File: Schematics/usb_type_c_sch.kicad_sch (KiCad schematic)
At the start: 4 parts, among them J2 USB_C_Receptacle

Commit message: began routing
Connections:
- net D+: now also D1.4; no longer D1.1
- net D-: now also D1.6; no longer D1.3
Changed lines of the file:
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@@
+	)
+	(junction
+		(at 151.13 81.28)
+		(diameter 0)
+		(color 0 0 0 0)
+	)
+	(junction
+		(at 121.92 134.62)
+		(diameter 0)
+		(color 0 0 0 0)
 	)
 	(junction
@@
 	)
 	(junction
-		(at 121.92 134.62)
-		(diameter 0)
-		(color 0 0 0 0)
-	)
-	(junction
-		(at 149.86 81.28)
-		(diameter 0)
-		(color 0 0 0 0)
-	)
-	(junction
 		(at 147.32 81.28)
 		(diameter 0)
@@
 	(wire
 		(pts
-			(xy 147.32 81.28) (xy 149.86 81.28)
+			(xy 147.32 81.28) (xy 151.13 81.28)
 		)
 		(stroke
@@
 	(wire
 		(pts
-			(xy 153.67 86.36) (xy 160.02 86.36)
-		)
-		(stroke
-			(width 0)
-			(type default)
-		)
-	)
-	(wire
-		(pts
 			(xy 193.04 82.55) (xy 193.04 83.82)
 		)
@@
 	(wire
 		(pts
+			(xy 158.75 81.28) (xy 160.02 81.28)
+		)
+		(stroke
+			(width 0)
+			(type default)
+		)
+	)
+	(wire
+		(pts
 			(xy 147.32 80.01) (xy 147.32 81.28)
 		)
@@
 	(wire
 		(pts
-			(xy 149.86 81.28) (xy 153.67 81.28)
-		)
-		(stroke
-			(width 0)
-			(type default)
-		)
-	)
-	(wire
-		(pts
 			(xy 140.97 80.01) (xy 147.32 80.01)
 		)
@@
 	(wire
 		(pts
-			(xy 149.86 83.82) (xy 160.02 83.82)
+			(xy 151.13 81.28) (xy 151.13 78.74)
+		)
+		(stroke
+			(width 0)
+			(type default)
+		)
+	)
+	(wire
+		(pts
+			(xy 158.75 86.36) (xy 158.75 81.28)
 		)
 		(stroke
@@
 	(wire
 		(pts
+			(xy 151.13 78.74) (xy 160.02 78.74)
+		)
+		(stroke
+			(width 0)
+			(type default)
+		)
+	)
+	(wire
+		(pts
 			(xy 147.32 82.55) (xy 140.97 82.55)
 		)
@@
 	(wire
 		(pts
-			(xy 149.86 81.28) (xy 149.86 83.82)
-		)
-		(stroke
-			(width 0)
-			(type default)
-		)
-	)
-	(wire
-		(pts
 			(xy 144.78 63.5) (xy 144.78 67.31)
 		)
@@
 	(wire
 		(pts
+			(xy 151.13 81.28) (xy 153.67 81.28)
+		)
+		(stroke
+			(width 0)
+			(type default)
+		)
+	)
+	(wire
+		(pts
 			(xy 147.32 81.28) (xy 147.32 82.55)
 		)
 		(stroke
+			(width 0)
+			(type default)
+		)
+	)
+	(wire
+		(pts
+			(xy 153.67 86.36) (xy 158.75 86.36)
+		)
+		(stroke

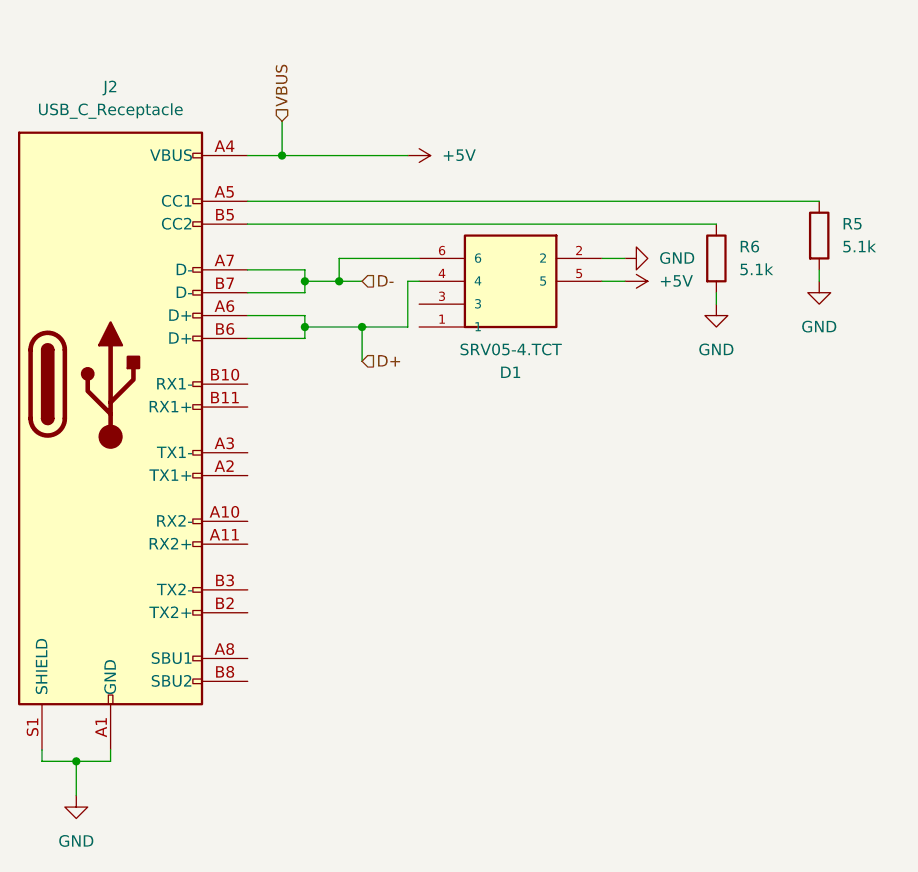
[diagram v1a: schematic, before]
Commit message: fixing routing redefining layout
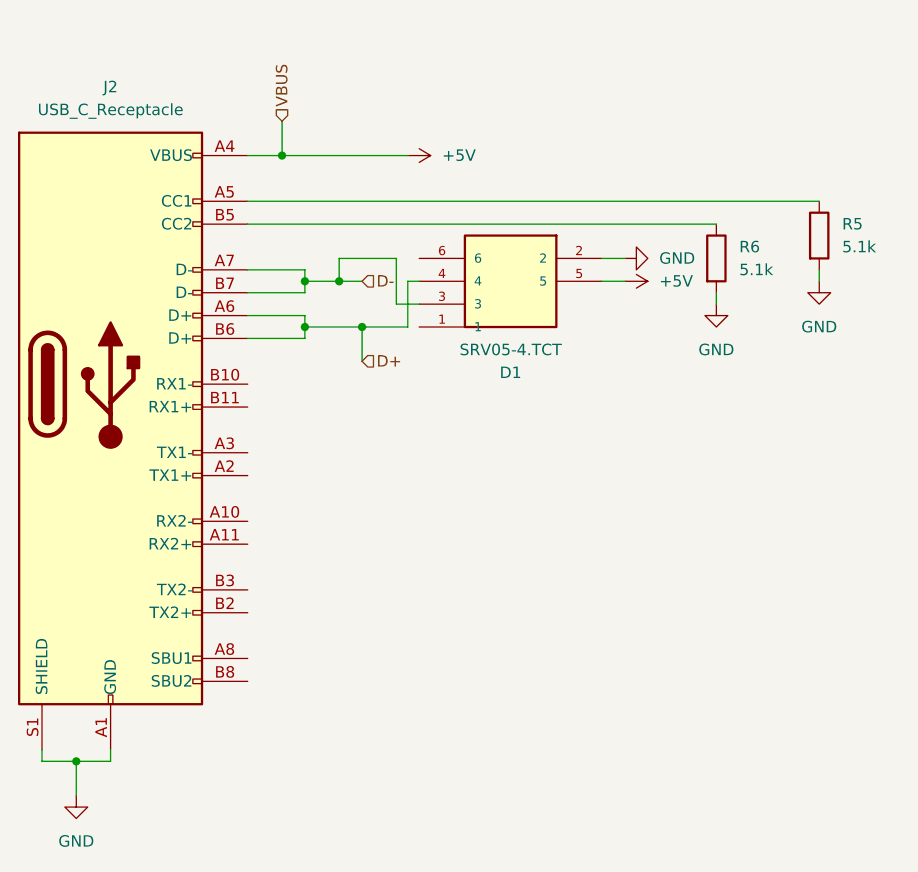
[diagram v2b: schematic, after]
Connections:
- net D-: now also D1.3; no longer D1.6
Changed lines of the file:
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@@
+	(wire
+		(pts
+			(xy 157.48 78.74) (xy 157.48 83.82)
+		)
+		(stroke
+			(width 0)
+			(type default)
+		)
+	)
 	(wire
 		(pts
@@
 	(wire
 		(pts
+			(xy 147.32 80.01) (xy 147.32 81.28)
+		)
+		(stroke
+			(width 0)
+			(type default)
+		)
+	)
+	(wire
+		(pts
+			(xy 140.97 67.31) (xy 144.78 67.31)
+		)
+		(stroke
+			(width 0)
+			(type default)
+		)
+	)
+	(wire
+		(pts
+			(xy 151.13 78.74) (xy 157.48 78.74)
+		)
+		(stroke
+			(width 0)
+			(type default)
+		)
+	)
+	(wire
+		(pts
+			(xy 140.97 85.09) (xy 147.32 85.09)
+		)
+		(stroke
+			(width 0)
+			(type default)
+		)
+	)
+	(wire
+		(pts
+			(xy 147.32 86.36) (xy 147.32 87.63)
+		)
+		(stroke
+			(width 0)
+			(type default)
+		)
+	)
+	(wire
+		(pts
+			(xy 140.97 74.93) (xy 193.04 74.93)
+		)
+		(stroke
+			(width 0)
+			(type default)
+		)
+	)
+	(wire
+		(pts
+			(xy 121.92 134.62) (xy 121.92 138.43)
+		)
+		(stroke
+			(width 0)
+			(type default)
+		)
+	)
+	(wire
+		(pts
 			(xy 158.75 81.28) (xy 160.02 81.28)
 		)
@@
 	(wire
 		(pts
-			(xy 147.32 80.01) (xy 147.32 81.28)
-		)
-		(stroke
-			(width 0)
-			(type default)
-		)
-	)
-	(wire
-		(pts
-			(xy 140.97 67.31) (xy 144.78 67.31)
-		)
-		(stroke
-			(width 0)
-			(type default)
-		)
-	)
-	(wire
-		(pts
-			(xy 140.97 85.09) (xy 147.32 85.09)
-		)
-		(stroke
-			(width 0)
-			(type default)
-		)
-	)
-	(wire
-		(pts
-			(xy 147.32 86.36) (xy 147.32 87.63)
-		)
-		(stroke
-			(width 0)
-			(type default)
-		)
-	)
-	(wire
-		(pts
-			(xy 140.97 74.93) (xy 193.04 74.93)
-		)
-		(stroke
-			(width 0)
-			(type default)
-		)
-	)
-	(wire
-		(pts
-			(xy 121.92 134.62) (xy 121.92 138.43)
-		)
-		(stroke
-			(width 0)
-			(type default)
-		)
-	)
-	(wire
-		(pts
 			(xy 140.97 80.01) (xy 147.32 80.01)
 		)
@@
 	(wire
 		(pts
+			(xy 153.67 90.17) (xy 153.67 86.36)
+		)
+		(stroke
+			(width 0)
+			(type default)
+		)
+	)
+	(wire
+		(pts
+			(xy 118.11 134.62) (xy 121.92 134.62)
+		)
+		(stroke
+			(width 0)
+			(type default)
+		)
+	)
+	(wire
+		(pts
+			(xy 147.32 85.09) (xy 147.32 86.36)
+		)
+		(stroke
+			(width 0)
+			(type default)
+		)
+	)
+	(wire
+		(pts
+			(xy 182.88 78.74) (xy 180.34 78.74)
+		)
+		(stroke
+			(width 0)
+			(type default)
+		)
+	)
+	(wire
+		(pts
+			(xy 204.47 80.01) (xy 204.47 81.28)
+		)
+		(stroke
+			(width 0)
+			(type default)
+		)
+	)
+	(wire
+		(pts
+			(xy 118.11 134.62) (xy 118.11 133.35)
+		)
+		(stroke
+			(width 0)
+			(type default)
+		)
+	)
+	(wire
+		(pts
+			(xy 147.32 82.55) (xy 140.97 82.55)
+		)
+		(stroke
+			(width 0)
+			(type default)
+		)
+	)
+	(wire
+		(pts
+			(xy 144.78 63.5) (xy 144.78 67.31)
+		)
+		(stroke
+			(width 0)
+			(type default)
+		)
+	)
+	(wire
+		(pts
+			(xy 125.73 134.62) (xy 125.73 133.35)
+		)
+		(stroke
+			(width 0)
+			(type default)
+		)
+	)
+	(wire
+		(pts
+			(xy 151.13 81.28) (xy 153.67 81.28)
+		)
+		(stroke
+			(width 0)
+			(type default)
+		)
+	)
+	(wire
+		(pts
+			(xy 157.48 83.82) (xy 160.02 83.82)
+		)
+		(stroke
+			(width 0)
+			(type default)
+		)
+	)
+	(wire
+		(pts
 			(xy 158.75 86.36) (xy 158.75 81.28)
 		)
 		(stroke
-			(width 0)
-			(type default)
-		)
-	)
-	(wire
-		(pts
-			(xy 153.67 90.17) (xy 153.67 86.36)
-		)
-		(stroke
-			(width 0)
-			(type default)
-		)
-	)
-	(wire
-		(pts
-			(xy 118.11 134.62) (xy 121.92 134.62)
-		)
-		(stroke
-			(width 0)
-			(type default)
-		)
-	)
-	(wire
-		(pts
-			(xy 147.32 85.09) (xy 147.32 86.36)
-		)
-		(stroke
-			(width 0)
-			(type default)
-		)
-	)
-	(wire
-		(pts
-			(xy 182.88 78.74) (xy 180.34 78.74)
-		)
-		(stroke
-			(width 0)
-			(type default)
-		)
-	)
-	(wire
-		(pts
-			(xy 204.47 80.01) (xy 204.47 81.28)
-		)
-		(stroke
-			(width 0)
-			(type default)
-		)
-	)
-	(wire
-		(pts
-			(xy 118.11 134.62) (xy 118.11 133.35)
-		)
-		(stroke
-			(width 0)
-			(type default)
-		)
-	)
-	(wire
-		(pts
-			(xy 151.13 78.74) (xy 160.02 78.74)
-		)
-		(stroke
-			(width 0)
-			(type default)
-		)
-	)
-	(wire
-		(pts
-			(xy 147.32 82.55) (xy 140.97 82.55)
-		)
-		(stroke
-			(width 0)
-			(type default)
-		)
-	)
-	(wire
-		(pts
-			(xy 144.78 63.5) (xy 144.78 67.31)
-		)
-		(stroke
-			(width 0)
-			(type default)
-		)
-	)
-	(wire
-		(pts
-			(xy 125.73 134.62) (xy 125.73 133.35)
-		)
-		(stroke
-			(width 0)
-			(type default)
-		)
-	)
-	(wire
-		(pts
-			(xy 151.13 81.28) (xy 153.67 81.28)
-		)
-		(stroke

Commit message: routing taking place only USB to do
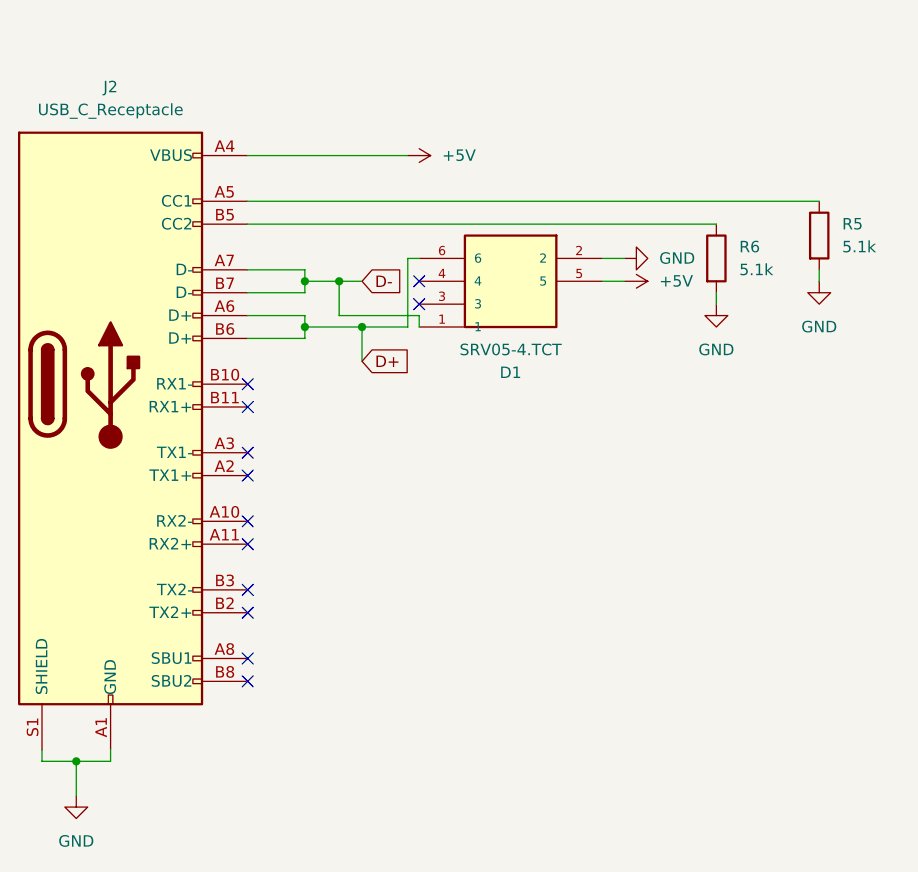
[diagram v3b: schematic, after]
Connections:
- net D+: now also D1.6; no longer D1.4
- net D-: now also D1.1; no longer D1.3
- no-connect marks 0 -> 12

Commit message: Cleaned up schematic added ocilator added jtag 10 pin begining routing again
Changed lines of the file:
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@@
 		)
 	)
-	(global_label "D-"
+	(hierarchical_label "D-"
 		(shape input)
 		(at 153.67 81.28 0)
-		(fields_autoplaced yes)
 		(effects
 			(font
@@
 			(justify left)
 		)
-		(property "Intersheetrefs" "${INTERSHEET_REFS}"
-			(at 159.4976 81.28 0)
-			(effects
-				(font
-					(size 1.27 1.27)
-				)
-				(justify left)
-				(hide yes)
-			)
-		)
 	)
-	(global_label "D+"
+	(hierarchical_label "D+"
 		(shape input)
 		(at 153.67 90.17 0)
-		(fields_autoplaced yes)
 		(effects
 			(font
@@
 			(justify left)
 		)
-		(property "Intersheetrefs" "${INTERSHEET_REFS}"
-			(at 159.4976 90.17 0)
-			(effects
-				(font
-					(size 1.27 1.27)
-				)
-				(justify left)
-				(hide yes)
-			)
-		)
 	)

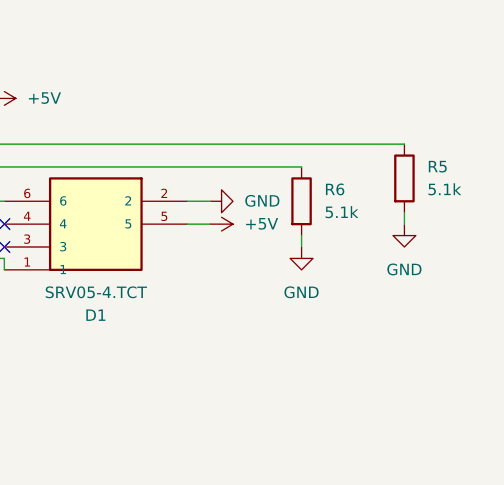
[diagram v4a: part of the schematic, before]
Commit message: added LCSC numbers and generated BOM, fixed schematic
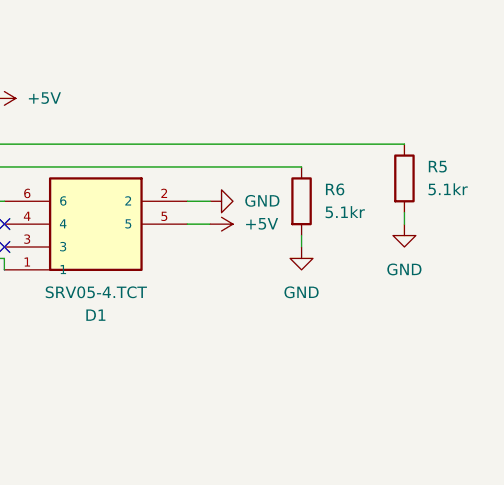
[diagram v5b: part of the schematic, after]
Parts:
- D1: LCSC (none) -> C13612
- J2: LCSC (none) -> C49566391
- R5, R6: value 5.1k -> 5.1kr; LCSC (none) -> C27834
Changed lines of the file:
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@@
+			)
+		)
+		(property "LCSC" "C49566391"
+			(at 125.73 92.71 0)
+			(effects
+				(font
+					(size 1.27 1.27)
+				)
+				(hide yes)
 			)
 		)
@@
 			)
 		)
+		(property "LCSC" "C13612"
+			(at 180.34 83.82 0)
+			(effects
+				(font
+					(size 1.27 1.27)
+				)
+				(hide yes)
+			)
+		)
 		(pin "4"
 		)
@@
 			)
 		)
-		(property "Value" "5.1k"
+		(property "Value" "5.1kr"
 			(at 195.58 80.0099 0)
 			(effects
@@
 		)
 		(property "Description" "Resistor"
+			(at 193.04 78.74 0)
+			(effects
+				(font
+					(size 1.27 1.27)
+				)
+				(hide yes)
+			)
+		)
+		(property "LCSC" "C27834"
 			(at 193.04 78.74 0)
 			(effects
@@
 			)
 		)
-		(property "Value" "5.1k"
+		(property "Value" "5.1kr"
 			(at 207.01 77.4699 0)
 			(effects
@@
 			(at 204.47 76.2 0)
 			(effects
+				(font
+					(size 1.27 1.27)
+				)
+				(hide yes)
+			)
+		)
+		(property "LCSC" "C27834"
+			(at 204.47 76.2 0)
+			(effects

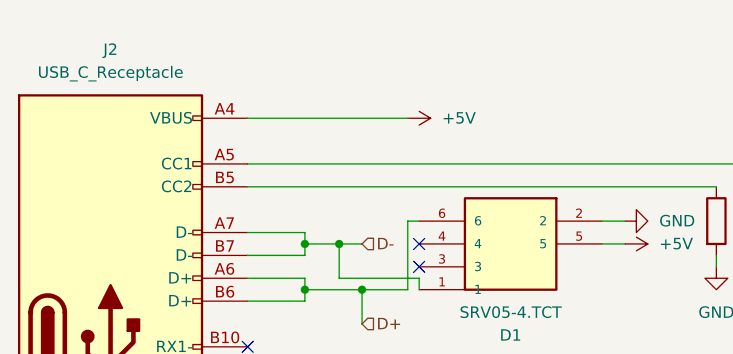
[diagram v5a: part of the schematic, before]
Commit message: Ran ERC added Pwr Flags
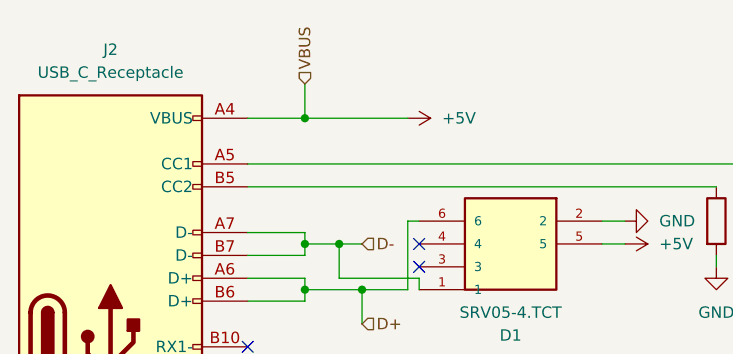
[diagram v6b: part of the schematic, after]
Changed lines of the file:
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@@
+	)
+	(junction
+		(at 147.32 67.31)
+		(diameter 0)
+		(color 0 0 0 0)
 	)
 	(junction
@@
 	(wire
 		(pts
-			(xy 140.97 67.31) (xy 158.75 67.31)
+			(xy 140.97 67.31) (xy 147.32 67.31)
+		)
+		(stroke
+			(width 0)
+			(type default)
+		)
+	)
+	(wire
+		(pts
+			(xy 147.32 67.31) (xy 158.75 67.31)
 		)
 		(stroke
@@
 		(pts
 			(xy 140.97 72.39) (xy 204.47 72.39)
+		)
+		(stroke
+			(width 0)
+			(type default)
+		)
+	)
+	(wire
+		(pts
+			(xy 147.32 63.5) (xy 147.32 67.31)
 		)
 		(stroke
@@
 		(effects
 			(font
+				(size 1.27 1.27)
+			)
+			(justify left)
+		)
+	)
+	(hierarchical_label "VBUS"
+		(shape input)
+		(at 147.32 63.5 90)
+		(effects
+			(font
